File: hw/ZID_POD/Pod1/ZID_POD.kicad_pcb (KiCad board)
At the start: 2 copper layers, 52.8 x 19.3 mm, 2 parts, among them J1 Z80-POD

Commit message: POD PCB 4 layouts
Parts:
- Z80-SKT1: renamed from SKT1; footprint Package_DIP:DIP-40_W15.24mm -> Package_DIP:DIP-40_W15.24mm_Socket
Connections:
- J1 pad 30: /PWR -> /GND
- Z80-SKT1 pad 11: /PWR -> unconnected-(Z80-SKT1-GND/NC-Pad11)
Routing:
- net /GND: track 10.5 -> 35.6 mm
- net /PWR: track 14.2 -> 0.00 mm, vias 1 -> 0
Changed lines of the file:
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@@
 	(title_block
 		(title "Z80 In-circuit Debugger (ZID) POD (1)")
-		(date "2026-04-12")
+		(date "2026-04-13")
 		(rev "PR1.0")
 		(company "SilkyDESIGN")
@@
 	(net 3 "/GND")
 	(net 4 "/A5")
-	(net 5 "/PWR")
+	(net 5 "unconnected-(Z80-SKT1-GND{slash}NC-Pad11)")
 	(net 6 "/RST-")
 	(net 7 "/A6")
@@
 	(net 39 "/IORQ-")
 	(net 40 "/A3")
-	(footprint "Package_DIP:DIP-40_W15.24mm"
+	(footprint "Package_DIP:DIP-40_W15.24mm_Socket"
 		(locked yes)
 		(layer "F.Cu")
 		(at 92.202 109.474 90)
-		(descr "40-lead though-hole mounted DIP package, row spacing 15.24mm (600 mils)")
-		(tags "THT DIP DIL PDIP 2.54mm 15.24mm 600mil")
-		(property "Reference" "SKT1"
-			(at 7.62 0.762 90)
+		(descr "40-lead though-hole mounted DIP package, row spacing 15.24mm (600 mils), Socket")
+		(tags "THT DIP DIL PDIP 2.54mm 15.24mm 600mil Socket")
+		(property "Reference" "Z80-SKT1"
+			(at 7.62 -2.33 90)
 			(layer "F.SilkS")
 			(effects
@@
 			)
 		)
-		(property "Description" "Plugs into the Z80 socket on target"
+		(property "Description" "Connect Z80 to Target via Cable"
 			(at 0 0 90)
 			(layer "F.Fab")
@@
 			)
 		)
-		(property "PIN_NOTE" "BIDIRECTIONAL pins are OUT on Z80, IN on DEBUGGER"
+		(property "PIN_NOTE" "BIDIRECTIONAL pins are OUT on Z80, IN on TARGET"
 			(at 0 0 90)
 			(unlocked yes)
@@
 		(attr through_hole)
 		(fp_line
-			(start 14.079999 -1.33)
-			(end 8.619999 -1.33)
+			(start 14.08 -1.33)
+			(end 8.62 -1.33)
 			(stroke
 				(width 0.12)
@@
 		(fp_line
 			(start 14.08 49.59)
-			(end 14.079999 -1.33)
+			(end 14.08 -1.33)
 			(stroke
 				(width 0.12)
@@
 			(layer "F.SilkS")
 		)
+		(fp_rect
+			(start -1.33 -1.39)
+			(end 16.57 49.65)
+			(stroke
+				(width 0.12)
+				(type solid)
+			)
+			(fill no)
+			(layer "F.SilkS")
+		)
 		(fp_arc
-			(start 8.619999 -1.33)
+			(start 8.62 -1.33)
 			(mid 7.62 -0.33)
 			(end 6.62 -1.33)
@@
 			(layer "F.SilkS")
 		)
-		(fp_poly
-			(pts
-				(xy -1.05 -1.529999) (xy 16.29 -1.53) (xy 16.29 49.78) (xy -1.050001 49.78)
-			)
+		(fp_rect
+			(start -1.53 -1.59)
+			(end 16.77 49.84)
 			(stroke
 				(width 0.05)
@@
 		)
 		(fp_line
-			(start 1.255 -1.270001)
-			(end 14.985001 -1.27)
-			(stroke
-				(width 0.1)
-				(type solid)
-			)
-			(layer "F.Fab")
-		)
-		(fp_line
-			(start 14.985001 -1.27)
+			(start 14.985 -1.27)
 			(end 14.985 49.53)
 			(stroke
@@
 		)
 		(fp_line
+			(start 1.255 -1.27)
+			(end 14.985 -1.27)
+			(stroke
+				(width 0.1)
+				(type solid)
+			)
+			(layer "F.Fab")
+		)
+		(fp_line
 			(start 0.255 -0.27)
-			(end 1.255 -1.270001)
+			(end 1.255 -1.27)
 			(stroke
 				(width 0.1)
@@
 			(layer "F.Fab")
 		)
+		(fp_rect
+			(start -1.27 -1.33)
+			(end 16.51 49.59)
+			(stroke
+				(width 0.1)
+				(type solid)
+			)
+			(fill no)
+			(layer "F.Fab")
+		)
 		(fp_text user "${REFERENCE}"
-			(at 7.62 24.13 0)
+			(at 7.62 24.13 180)
 			(layer "F.Fab")
 			(effects
@@
 		)
 		(pad "3" thru_hole circle
-			(at 0 5.079999 90)
+			(at 0 5.08 90)
 			(size 1.6 1.6)
 			(drill 0.8)
@@
 		)
 		(pad "8" thru_hole circle
-			(at 0 17.780001 90)
+			(at 0 17.78 90)
 			(size 1.6 1.6)
 			(drill 0.8)
@@
 			(layers "*.Cu" "*.Mask")
 			(remove_unused_layers no)
-			(net 5 "/PWR")
-			(pinfunction "5V")
-			(pintype "power_in")
+			(net 5 "unconnected-(Z80-SKT1-GND{slash}NC-Pad11)")
+			(pinfunction "GND/NC")
+			(pintype "power_in+no_connect")
 		)
 		(pad "12" thru_hole circle
-			(at 0 27.939999 90)
+			(at 0 27.94 90)
 			(size 1.6 1.6)
 			(drill 0.8)
@@
 		)
 		(pad "16" thru_hole circle
-			(at 0 38.099999 90)
+			(at 0 38.1 90)
 			(size 1.6 1.6)
 			(drill 0.8)
@@
 		)
 		(pad "17" thru_hole circle
-			(at 0 40.640001 90)
+			(at 0 40.64 90)
 			(size 1.6 1.6)
 			(drill 0.8)
@@
 		)
 		(embedded_fonts no)
-		(model "${KICAD9_3DMODEL_DIR}/Package_DIP.3dshapes/DIP-40_W15.24mm.step"
+		(model "${KICAD9_3DMODEL_DIR}/Package_DIP.3dshapes/DIP-40_W15.24mm_Socket.step"
 			(offset
 				(xyz 0 0 0)
@@
 			(size 0.3 1.3)
 			(layers "F.Cu" "F.Mask" "F.Paste")
-			(net 5 "/PWR")
-			(pinfunction "5V")
+			(net 3 "/GND")
+			(pinfunction "GND/NC")
 			(pintype "power_in")
 		)
@@
 			)
 		)
+	)
+	(gr_rect
+		(start 91.186 110.49)
+		(end 93.218 110.998)
+		(stroke
+			(width 0.1)
+			(type solid)
+		)
+		(fill yes)
+		(layer "F.SilkS")
+	)
+	(gr_poly
+		(pts
+			(xy 128.524 106.172) (xy 129.032 105.664) (xy 129.032 106.68)
+		)
+		(stroke
+			(width 0.1)
+			(type solid)
+		)
+		(fill yes)
+		(layer "F.SilkS")
+	)
+	(gr_rect
+		(start 90.424 108.458)
+		(end 91.186 110.998)
+		(stroke
+			(width 0.1)
+			(type solid)
+		)
+		(fill yes)
+		(layer "F.SilkS")
 	)
 	(gr_poly
@@
 		)
 		(layer "Edge.Cuts")
+	)
+	(gr_text "ZID CBL\nPIN-1"
+		(at 129.54 108.204 0)
+		(layer "F.SilkS")
+		(effects
+			(font
+				(size 1 1)
+				(thickness 0.2)
+				(bold yes)
+			)
+			(justify left bottom)
+		)
 	)
 	(gr_text "ZID CBL\nPIN-1"
@@
 	)
 	(segment
+		(start 131.403 93.77795)
+		(end 130.75805 93.133)
+		(width 0.2)
+		(layer "F.Cu")
+		(net 3)
+	)
+	(segment
 		(start 113.80774 95.828991)
 		(end 113.809152 95.828991)
@@
 	)
 	(segment
+		(start 121.436 98.806)
+		(end 121.436 97.904)
+		(width 0.2)
+		(layer "F.Cu")
+		(net 3)
+	)
+	(segment
 		(start 112.436 97.200731)
 		(end 113.80774 95.828991)
@@
 	)
 	(segment
+		(start 121.243 93.133)
+		(end 120.142 94.234)
+		(width 0.2)
+		(layer "F.Cu")
+		(net 3)
+	)
+	(segment
+		(start 121.436 97.904)
+		(end 121.485 97.855)
+		(width 0.2)
+		(layer "F.Cu")
+		(net 3)
+	)
+	(segment
 		(start 118.548 95.828)
 		(end 120.142 94.234)
@@
 	)
 	(segment
+		(start 121.485 97.855)
+		(end 128.23805 97.855)
+		(width 0.2)
+		(layer "F.Cu")
+		(net 3)
+	)
+	(segment
+		(start 128.23805 97.855)
+		(end 131.403 94.69005)
+		(width 0.2)
+		(layer "F.Cu")
+		(net 3)
+	)
+	(segment
+		(start 131.403 94.69005)
+		(end 131.403 93.77795)
+		(width 0.2)
+		(layer "F.Cu")
+		(net 3)
+	)
+	(segment
+		(start 130.75805 93.133)
+		(end 121.243 93.133)
+		(width 0.2)
+		(layer "F.Cu")
+		(net 3)
+	)
+	(segment
 		(start 113.810145 95.828)
 		(end 118.548 95.828)
@@
 	)
 	(segment
-		(start 121.488297 106.979364)
-		(end 121.488297 107.297916)
-		(width 0.2)
-		(layer "F.Cu")
-		(net 5)
-	)
-	(segment
-		(start 121.535 99.8912)
-		(end 121.733 100.0892)
-		(width 0.2)
-		(layer "F.Cu")
-		(net 5)
-	)
-	(segment
-		(start 121.535 99.757)
-		(end 121.535 99.8912)
-		(width 0.2)
-		(layer "F.Cu")
-		(net 5)
-	)
-	(segment
-		(start 121.733 106.734661)
-		(end 121.488297 106.979364)
-		(width 0.2)
-		(layer "F.Cu")
-		(net 5)
-	)
-	(segment
-		(start 121.733 100.0892)
-		(end 121.733 106.734661)
-		(width 0.2)
-		(layer "F.Cu")
-		(net 5)
-	)
-	(segment
-		(start 121.488297 107.297916)
-		(end 121.117737 107.668476)
-		(width 0.2)
-		(layer "F.Cu")
-		(net 5)
-	)
-	(segment
-		(start 121.117737 107.668476)
-		(end 121.117737 108.541024)
-		(width 0.2)
-		(layer "F.Cu")
-		(net 5)
-	)
-	(segment
-		(start 121.436 99.658)
-		(end 121.535 99.757)
-		(width 0.2)
-		(layer "F.Cu")
-		(net 5)
-	)
-	(segment
-		(start 121.436 98.806)
-		(end 121.436 99.658)
-		(width 0.2)
-		(layer "F.Cu")
-		(net 5)
-	)
-	(via
-		(at 121.117737 108.541024)
-		(size 0.6)
-		(drill 0.3)
-		(layers "F.Cu" "B.Cu")
-		(net 5)
-	)
-	(segment
-		(start 119.685949 108.373)
-		(end 120.949713 108.373)
-		(width 0.2)
-		(layer "B.Cu")
-		(net 5)
-	)
-	(segment
-		(start 118.11 108.966)
-		(end 119.092949 108.966)
-		(width 0.2)
-		(layer "B.Cu")
-		(net 5)
-	)
-	(segment
-		(start 117.602 109.474)
-		(end 118.11 108.966)
-		(width 0.2)
-		(layer "B.Cu")
-		(net 5)
-	)
-	(segment
-		(start 120.949713 108.373)
-		(end 121.117737 108.541024)
-		(width 0.2)
-		(layer "B.Cu")
-		(net 5)
-	)
-	(segment
-		(start 119.092949 108.966)
-		(end 119.685949 108.373)
-		(width 0.2)
-		(layer "B.Cu")
-		(net 5)
-	)
-	(segment

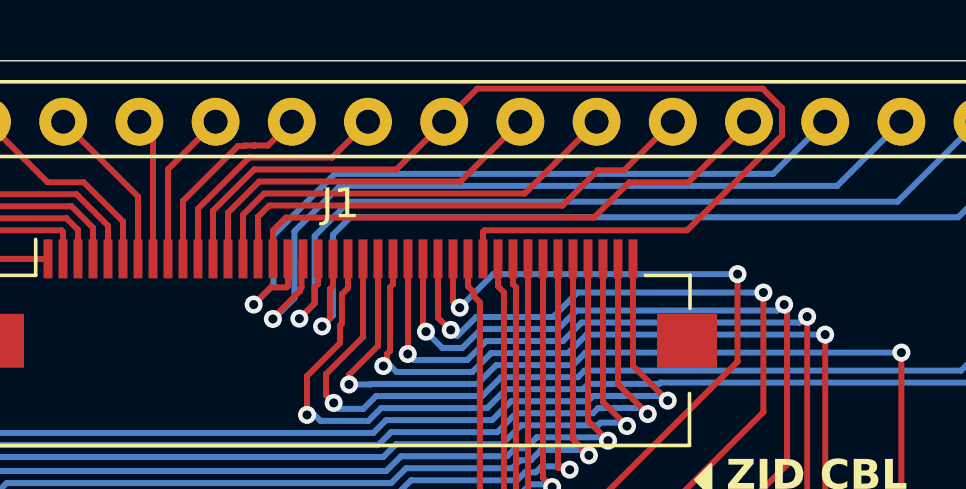
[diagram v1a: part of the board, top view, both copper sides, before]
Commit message: POD PCB increase GND trace width
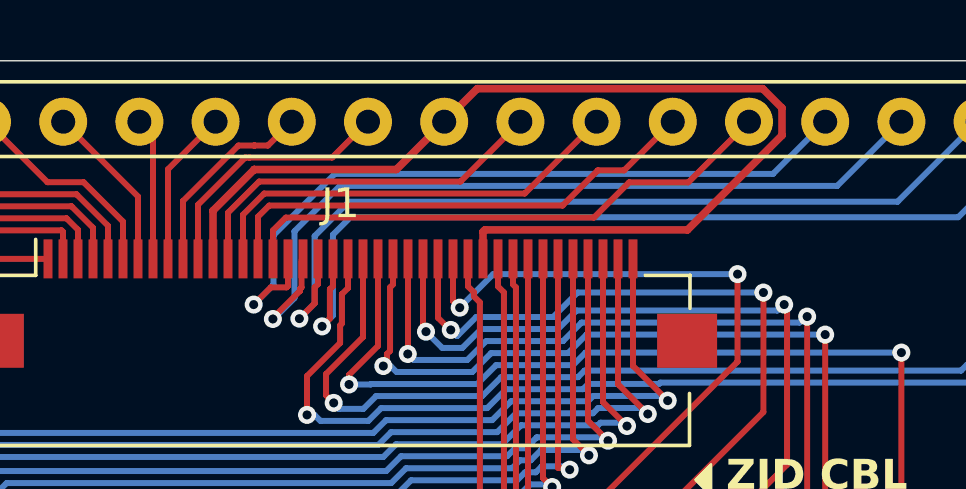
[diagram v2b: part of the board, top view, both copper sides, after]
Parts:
- J1: value Z80-POD -> Z80-POD (1)
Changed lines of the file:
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@@
 			)
 		)
-		(property "Value" "Z80-POD"
+		(property "Value" "Z80-POD (1)"
 			(at 0 5.6 0)
 			(layer "B.SilkS")
@@
 	)
 	(segment
+		(start 113.80774 95.828991)
+		(end 113.809152 95.828991)
+		(width 0.254)
+		(layer "F.Cu")
+		(net 3)
+	)
+	(segment
+		(start 112.436 97.200731)
+		(end 113.80774 95.828991)
+		(width 0.254)
+		(layer "F.Cu")
+		(net 3)
+	)
+	(segment
+		(start 113.809152 95.828991)
+		(end 113.810145 95.828)
+		(width 0.254)
+		(layer "F.Cu")
+		(net 3)
+	)
+	(segment
+		(start 118.548 95.828)
+		(end 120.142 94.234)
+		(width 0.254)
+		(layer "F.Cu")
+		(net 3)
+	)
+	(segment
+		(start 112.436 98.806)
+		(end 112.436 97.200731)
+		(width 0.254)
+		(layer "F.Cu")
+		(net 3)
+	)
+	(segment
 		(start 131.403 93.77795)
 		(end 130.75805 93.133)
-		(width 0.2)
+		(width 0.254)
 		(layer "F.Cu")
 		(net 3)
 	)
 	(segment
-		(start 113.80774 95.828991)
-		(end 113.809152 95.828991)
-		(width 0.2)
+		(start 121.4992 97.8408)
+		(end 128.25225 97.8408)
+		(width 0.254)
 		(layer "F.Cu")
 		(net 3)
@@
 		(start 121.436 98.806)
 		(end 121.436 97.904)
-		(width 0.2)
+		(width 0.254)
 		(layer "F.Cu")
 		(net 3)
 	)
 	(segment
-		(start 112.436 97.200731)
-		(end 113.80774 95.828991)
-		(width 0.2)
+		(start 130.75805 93.133)
+		(end 121.243 93.133)
+		(width 0.254)
 		(layer "F.Cu")
 		(net 3)
 	)
 	(segment
-		(start 113.809152 95.828991)
-		(end 113.810145 95.828)
-		(width 0.2)
+		(start 128.25225 97.8408)
+		(end 131.403 94.69005)
+		(width 0.254)
+		(layer "F.Cu")
+		(net 3)
+	)
+	(segment
+		(start 121.436 97.904)
+		(end 121.4992 97.8408)
+		(width 0.254)
 		(layer "F.Cu")
 		(net 3)
@@
 		(start 121.243 93.133)
 		(end 120.142 94.234)
-		(width 0.2)
+		(width 0.254)
 		(layer "F.Cu")
 		(net 3)
 	)
 	(segment
-		(start 121.436 97.904)
-		(end 121.485 97.855)
-		(width 0.2)
-		(layer "F.Cu")
-		(net 3)
-	)
-	(segment
-		(start 118.548 95.828)
-		(end 120.142 94.234)
-		(width 0.2)
-		(layer "F.Cu")
-		(net 3)
-	)
-	(segment
-		(start 112.436 98.806)
-		(end 112.436 97.200731)
-		(width 0.2)
-		(layer "F.Cu")
-		(net 3)
-	)
-	(segment
-		(start 121.485 97.855)
-		(end 128.23805 97.855)
-		(width 0.2)
-		(layer "F.Cu")
-		(net 3)
-	)
-	(segment
-		(start 128.23805 97.855)
-		(end 131.403 94.69005)
-		(width 0.2)
+		(start 113.810145 95.828)
+		(end 118.548 95.828)
+		(width 0.254)
 		(layer "F.Cu")
 		(net 3)
@@
 		(start 131.403 94.69005)
 		(end 131.403 93.77795)
-		(width 0.2)
-		(layer "F.Cu")
-		(net 3)
-	)
-	(segment
-		(start 130.75805 93.133)
-		(end 121.243 93.133)
-		(width 0.2)
-		(layer "F.Cu")
-		(net 3)
-	)
-	(segment
-		(start 113.810145 95.828)
-		(end 118.548 95.828)
-		(width 0.2)
+		(width 0.254)
 		(layer "F.Cu")
 		(net 3)
@@
 	)
 	(segment
-		(start 111.936 98.806)
-		(end 111.936 97.135045)
+		(start 113.643466 95.428991)
+		(end 113.644459 95.427998)
 		(width 0.2)
 		(layer "F.Cu")
@@
 	)
 	(segment
-		(start 111.936 97.135045)
-		(end 113.642055 95.428991)
+		(start 111.936 98.806)
+		(end 111.936 97.0044)
 		(width 0.2)
 		(layer "F.Cu")
@@
 	)
 	(segment
-		(start 113.643466 95.428991)
-		(end 113.644459 95.427998)
+		(start 111.936 97.0044)
+		(end 113.511409 95.428991)
 		(width 0.2)
 		(layer "F.Cu")
@@
 	)
 	(segment
-		(start 113.642055 95.428991)
+		(start 113.511409 95.428991)
 		(end 113.643466 95.428991)
 		(width 0.2)
@@
 	)
 	(segment
+		(start 111.436 96.87705)
+		(end 111.436 98.806)
+		(width 0.2)
+		(layer "F.Cu")
+		(net 13)
+	)
+	(segment
+		(start 113.810162 95.027984)
+		(end 113.285066 95.027984)
+		(width 0.2)
+		(layer "F.Cu")
+		(net 13)
+	)
+	(segment
+		(start 113.285066 95.027984)
+		(end 111.436 96.87705)
+		(width 0.2)
+		(layer "F.Cu")
+		(net 13)
+	)
+	(segment
 		(start 113.810177 95.027988)
 		(end 113.810166 95.027988)
@@
 	)
 	(segment
+		(start 113.810166 95.027988)
+		(end 113.810162 95.027984)
+		(width 0.2)
+		(layer "F.Cu")
+		(net 13)
+	)
+	(segment
+		(start 114.268008 95.027992)
+		(end 113.810181 95.027992)
+		(width 0.2)
+		(layer "F.Cu")
+		(net 13)
+	)
+	(segment
 		(start 113.810181 95.027992)
 		(end 113.810177 95.027988)
@@
 	)
 	(segment
-		(start 113.47879 95.027984)
-		(end 113.459776 95.046998)
-		(width 0.2)
-		(layer "F.Cu")
-		(net 13)
-	)
-	(segment
-		(start 111.436 96.87705)
-		(end 111.436 98.806)
-		(width 0.2)
-		(layer "F.Cu")
-		(net 13)
-	)
-	(segment
-		(start 113.810162 95.027984)
-		(end 113.47879 95.027984)
-		(width 0.2)
-		(layer "F.Cu")
-		(net 13)
-	)
-	(segment
-		(start 114.268008 95.027992)
-		(end 113.810181 95.027992)
-		(width 0.2)
-		(layer "F.Cu")
-		(net 13)
-	)
-	(segment
-		(start 113.266054 95.046998)
-		(end 111.436 96.87705)
-		(width 0.2)
-		(layer "F.Cu")
-		(net 13)
-	)
-	(segment
-		(start 113.459776 95.046998)
-		(end 113.266054 95.046998)
-		(width 0.2)
-		(layer "F.Cu")
-		(net 13)
-	)
-	(segment
 		(start 115.062 94.234)
 		(end 114.268008 95.027992)
-		(width 0.2)
-		(layer "F.Cu")
-		(net 13)
-	)
-	(segment
-		(start 113.810166 95.027988)
-		(end 113.810162 95.027984)
 		(width 0.2)
 		(layer "F.Cu")
@@
 	)
 	(segment
-		(start 113.974416 96.228)
+		(start 113.974414 96.228)
 		(end 120.688 96.228)
 		(width 0.2)
@@
 	)
 	(segment
-		(start 112.936 97.266414)
-		(end 113.974416 96.228)
+		(start 120.688 96.228)
+		(end 122.682 94.234)
 		(width 0.2)
 		(layer "F.Cu")
@@
 	)
 	(segment
-		(start 120.688 96.228)
-		(end 122.682 94.234)
-		(width 0.2)
-		(layer "F.Cu")
+		(start 112.936 97.266414)
+		(end 113.974414 96.228)
+		(width 0.2)
+		(layer "F.Cu")
